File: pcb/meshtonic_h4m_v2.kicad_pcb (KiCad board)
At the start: 6 copper layers, 71.1 x 168.4 mm, 116 parts, among them J1 GROVE-CONNECTOR-DIP_4P-2.0_, J10 Conn_01x02, J11 Conn_01x02, J12 JST_2mm_LiPo, J13 Screw_Terminal_01x02, J14 Micro_SD_Card_passive_clk, J15 H4M_2x6_MDK, J2 GROVE-CONNECTOR-DIP-90D_4P-2.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, J3 GROVE-CONNECTOR-DIP_4P-2.0_, J4 GROVE-CONNECTOR-DIP_4P-2.0_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

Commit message: adds meshtastic firmware
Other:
- board text added: "MESHTONIC EXPANSION BOARD MADE IN ZIBURU · DONIBANE LOHIZUNE · PAYS BASQUE FIRMWARE : https://github.com/bxrf"
- board text removed: "MESHTONIC EXPANSION BOARD MADE IN ZIBURU · DONIBANE LOHIZUNE · PAYS BASQUE FIRMWARE : https://github.com/Meshtonic ENGINEERING SAMPLE ___ / 5 NOT FOR SALE"
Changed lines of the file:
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@@
 		)
 	)
-	(gr_text "MESHTONIC EXPANSION BOARD\nMADE IN \nZIBURU · DONIBANE LOHIZUNE · PAYS BASQUE\n\nFIRMWARE : https://github.com/Meshtonic\nENGINEERING SAMPLE ___ / 5 NOT FOR SALE\n"
+	(gr_text "MESHTONIC EXPANSION BOARD\nMADE IN \nZIBURU · DONIBANE LOHIZUNE · PAYS BASQUE\nFIRMWARE : https://github.com/bxrf"
 		(at 141.39 167.03 0)
 		(layer "B.SilkS")

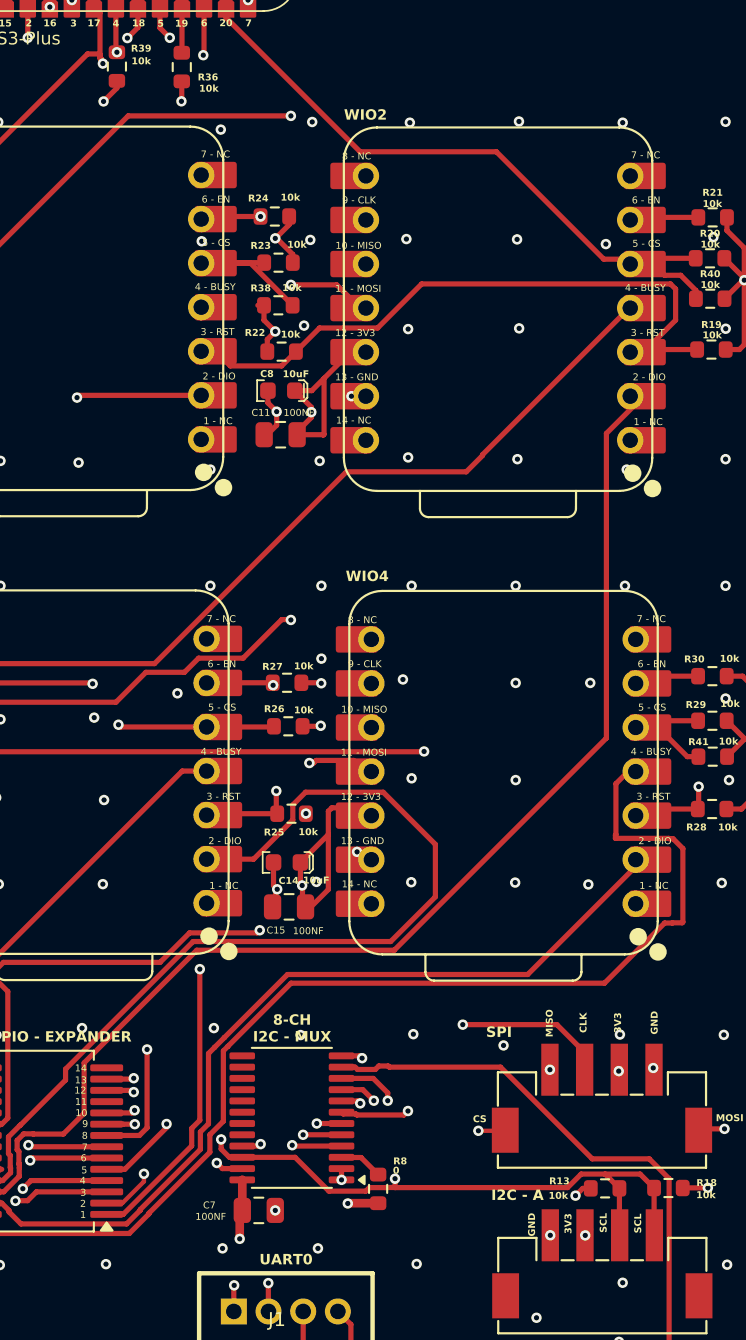
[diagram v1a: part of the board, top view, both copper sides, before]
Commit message: fixes SCL to SDA on J_AS1
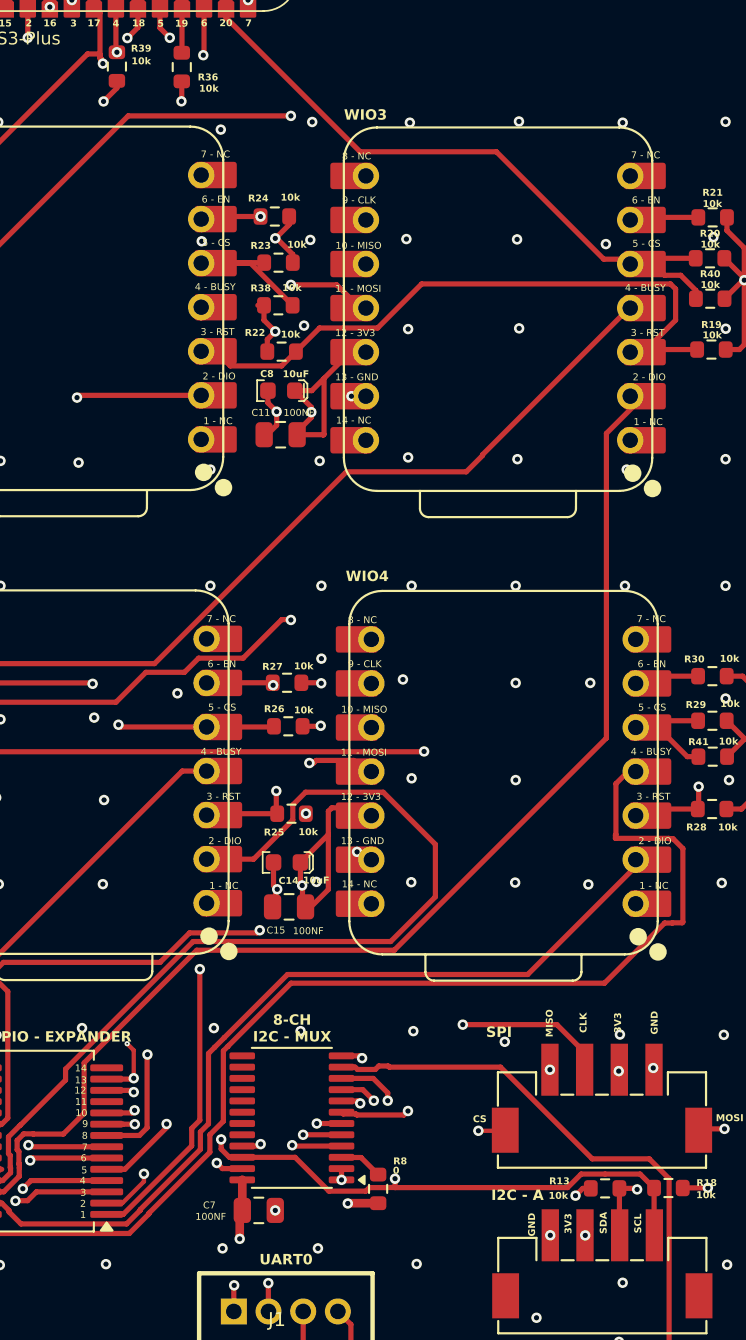
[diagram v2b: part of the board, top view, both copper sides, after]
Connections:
- J_AS1 pad 2: I2C_SCL -> I2C_SDA
- R13 pad 2: I2C_SCL -> I2C_SDA
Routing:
- net I2C_SDA: track 195.8 -> 234.4 mm, vias 5 -> 7
- net I2C_SCL: track 216.0 -> 212.2 mm
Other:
- board text added: "WIO3"
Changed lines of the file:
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@@
 			(size 3 1)
 			(layers "F.Cu" "F.Mask" "F.Paste")
-			(net "I2C_SCL")
+			(net "I2C_SDA")
 			(pinfunction "Pin_2_2")
 			(pintype "passive")
@@
 			(layers "F.Cu" "F.Mask" "F.Paste")
 			(roundrect_rratio 0.25)
-			(net "I2C_SCL")
+			(net "I2C_SDA")
 			(pintype "passive")
 		)
@@
 		)
 	)
-	(gr_text "SCL"
+	(gr_text "SDA"
 		(at 160.86 131.53 90)
 		(layer "F.SilkS")
@@
 		)
 	)
-	(gr_text "WIO2"
+	(gr_text "WIO3"
 		(at 145.9 68 0)
 		(layer "F.SilkS")
@@
 	)
 	(via
-		(at 155.1 121.3)
+		(at 155.171216 121.087332)
 		(size 0.6)
 		(drill 0.3)
@@
 	)
 	(via
-		(at 143.4 120.7)
+		(at 143.4 120.475)
 		(size 0.6)
 		(drill 0.3)
@@
 	)
 	(via
-		(at 149.9 120.65)
+		(at 149.9 120.475)
 		(size 0.6)
 		(drill 0.3)
@@
 	)
 	(segment
-		(start 134.109239 126.49)
-		(end 134.55 126.049239)
+		(start 128.47 17.07)
+		(end 128.47 18.707229)
 		(width 0.3)
 		(layer "F.Cu")
@@
 	)
 	(segment
-		(start 128.47 17.07)
-		(end 128.47 18.707229)
+		(start 134.109239 126.49)
+		(end 132.22 126.49)
 		(width 0.3)
 		(layer "F.Cu")
@@
 	)
 	(segment
-		(start 134.55 126.049239)
-		(end 134.55 121.53)
+		(start 132.19 126.49)
+		(end 132.18 126.5)
 		(width 0.3)
 		(layer "F.Cu")
@@
 	)
 	(segment
-		(start 132.19 126.49)
-		(end 132.18 126.5)
+		(start 134.57 121.929601)
+		(end 134.55 121.949601)
 		(width 0.3)
 		(layer "F.Cu")
@@
 	)
 	(segment
-		(start 132.22 126.49)
-		(end 134.109239 126.49)
+		(start 134.57 121.825)
+		(end 134.57 121.929601)
 		(width 0.3)
 		(layer "F.Cu")
@@
 	)
 	(segment
+		(start 134.55 126.049239)
+		(end 134.109239 126.49)
+		(width 0.3)
+		(layer "F.Cu")
+		(net "/Periferals/LED WIO 3")
+	)
+	(segment
 		(start 128.47 18.707229)
 		(end 128.522771 18.76)
@@
 		(net "/Periferals/LED WIO 3")
 	)
+	(segment
+		(start 134.55 121.949601)
+		(end 134.55 126.049239)
+		(width 0.3)
+		(layer "F.Cu")
+		(net "/Periferals/LED WIO 3")
+	)
 	(via
-		(at 134.55 121.53)
+		(at 134.57 121.825)
 		(size 0.6)
 		(drill 0.3)
@@
 	)
 	(segment
-		(start 136.42 26.57)
-		(end 128.61 18.76)
+		(start 138.383529 36.200586)
+		(end 136.42 34.237057)
 		(width 0.3)
 		(layer "In3.Cu")
@@
 	)
 	(segment
-		(start 138.383529 36.200586)
-		(end 136.42 34.237057)
+		(start 134.671048 121.579351)
+		(end 134.671048 48.993154)
 		(width 0.3)
 		(layer "In3.Cu")
@@
 	)
 	(segment
-		(start 136.42 34.237057)
-		(end 136.42 26.57)
+		(start 134.57 121.825)
+		(end 134.57 121.680399)
 		(width 0.3)
 		(layer "In3.Cu")
@@
 	)
 	(segment
-		(start 134.671048 121.408952)
-		(end 134.671048 48.993154)
+		(start 134.57 121.680399)
+		(end 134.671048 121.579351)
 		(width 0.3)
 		(layer "In3.Cu")
@@
 	)
 	(segment
-		(start 138.383529 45.280673)
-		(end 138.383529 36.200586)
+		(start 136.42 34.237057)
+		(end 136.42 26.57)
+		(width 0.3)
+		(layer "In3.Cu")
+		(net "/Periferals/LED WIO 3")
+	)
+	(segment
+		(start 136.42 26.57)
+		(end 128.61 18.76)
 		(width 0.3)
 		(layer "In3.Cu")
@@
 	)
 	(segment
-		(start 134.55 121.53)
-		(end 134.671048 121.408952)
+		(start 138.383529 45.280673)
+		(end 138.383529 36.200586)
 		(width 0.3)
 		(layer "In3.Cu")
@@
 	)
 	(segment
+		(start 133.77987 121.57987)
+		(end 133.77987 123.189998)
+		(width 0.25)
+		(layer "F.Cu")
+		(net "I2C_SDA")
+	)
+	(segment
 		(start 135.292177 61.031012)
 		(end 135.292177 62.638379)
@@
 	)
 	(segment
+		(start 162.64 129.54)
+		(end 162.7 129.6)
+		(width 0.3)
+		(layer "F.Cu")
+		(net "I2C_SDA")
+	)
+	(segment
 		(start 142.45 160.67)
 		(end 138.45 160.67)
@@
 	)
 	(segment
+		(start 133.4 121.2)
+		(end 133.77987 121.57987)
+		(width 0.25)
+		(layer "F.Cu")
+		(net "I2C_SDA")
+	)
+	(segment
 		(start 132.22 123.24)
 		(end 133.729868 123.24)
@@
 	)
 	(segment
+		(start 161.78 129.54)
+		(end 162.64 129.54)
+		(width 0.3)
+		(layer "F.Cu")
+		(net "I2C_SDA")
+	)
+	(segment
+		(start 161.78 129.54)
+		(end 161.78 132.22916)
+		(width 0.3)
+		(layer "F.Cu")
+		(net "I2C_SDA")
+	)
+	(segment
 		(start 138.892669 128.4)
 		(end 138.567669 128.075)
@@
 		(net "I2C_SDA")
 	)
+	(segment
+		(start 161.78 132.22916)
+		(end 161.795 132.24416)
+		(width 0.3)
+		(layer "F.Cu")
+		(net "I2C_SDA")
+	)
 	(via micro
 		(at 135.859044 63.205246)
@@
 		(net "I2C_SDA")
 	)
+	(via micro
+		(at 162.8 129.6)
+		(size 0.6)
+		(drill 0.3)
+		(layers "F.Cu" "In2.Cu")
+		(net "I2C_SDA")
+	)
+	(via micro
+		(at 133.4 121.2)
+		(size 0.3)
+		(drill 0.1)
+		(layers "F.Cu" "In2.Cu")
+		(net "I2C_SDA")
+	)
 	(via
 		(at 135.28 152.67)
@@
 	)
 	(segment
+		(start 162.8 129.6)
+		(end 154.4 121.2)
+		(width 0.25)
+		(layer "In2.Cu")
+		(net "I2C_SDA")
+	)
+	(segment
+		(start 154.4 121.2)
+		(end 133.4 121.2)
+		(width 0.25)
+		(layer "In2.Cu")
+		(net "I2C_SDA")
+	)
+	(segment
 		(start 138.96 54.872894)
 		(end 139.72 55.632894)
@@
 	)
 	(segment
-		(start 161.78 129.54)
-		(end 161.78 132.22916)
-		(width 0.3)
-		(layer "F.Cu")
-		(net "I2C_SCL")
-	)
-	(segment
 		(start 138.819938 127.272437)
 		(end 138.819938 126.716925)
@@
 	)
 	(segment
-		(start 160.955 128.715)
-		(end 161.78 129.54)
-		(width 0.3)
-		(layer "F.Cu")
-		(net "I2C_SCL")
-	)
-	(segment
 		(start 148.85 129.495)
 		(end 158.793883 129.495)
@@
 		(net "I2C_SCL")
 	)
-	(segment
-		(start 161.78 132.22916)
-		(end 161.795 132.24416)
-		(width 0.3)
-		(layer "F.Cu")
-		(net "I2C_SCL")
-	)
 	(via micro
 		(at 148.844362 128.981853)
@@
 	)
 	(segment
+		(start 144.05 120.205761)
+		(end 144.05 120.36)
+		(width 0.3)
+		(layer "In3.Cu")
+		(net "I2C_SCL")
+	)
+	(segment
 		(start 140.31 116.62)
-		(end 146.925 123.235)
+		(end 143.515 119.825)
 		(width 0.3)
 		(layer "In3.Cu")
@@
 	)
 	(segment
-		(start 148.26 142.98538)
-		(end 147.54 143.70538)
+		(start 140.31 66.73)
+		(end 140.31 116.62)
 		(width 0.3)
 		(layer "In3.Cu")
@@
 	)
 	(segment
-		(start 140.31 66.73)
-		(end 140.31 116.62)
+		(start 148.26 142.98538)
+		(end 147.54 143.70538)
+		(width 0.3)
+		(layer "In3.Cu")
+		(net "I2C_SCL")
+	)
+	(segment
+		(start 143.515 119.825)
+		(end 143.669239 119.825)
 		(width 0.3)
 		(layer "In3.Cu")
@@
 	)
 	(segment
+		(start 146.925 123.235)
+		(end 146.925 123.967028)
+		(width 0.3)
+		(layer "In3.Cu")
+		(net "I2C_SCL")
+	)
+	(segment
+		(start 143.669239 119.825)
+		(end 144.05 120.205761)
+		(width 0.3)
+		(layer "In3.Cu")
+		(net "I2C_SCL")
+	)
+	(segment
+		(start 144.05 120.36)
+		(end 146.925 123.235)
+		(width 0.3)
+		(layer "In3.Cu")
+		(net "I2C_SCL")
+	)
+	(segment
 		(start 148.26 128.981853)
 		(end 148.844362 128.981853)
@@
 		(width 0.3)
 		(layer "In3.Cu")
-		(net "I2C_SCL")
-	)
-	(segment
-		(start 146.925 123.235)
-		(end 146.925 123.967028)
-		(width 0.3)
-		(layer "In3.Cu")
